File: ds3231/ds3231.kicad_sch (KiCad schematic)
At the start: 0 parts

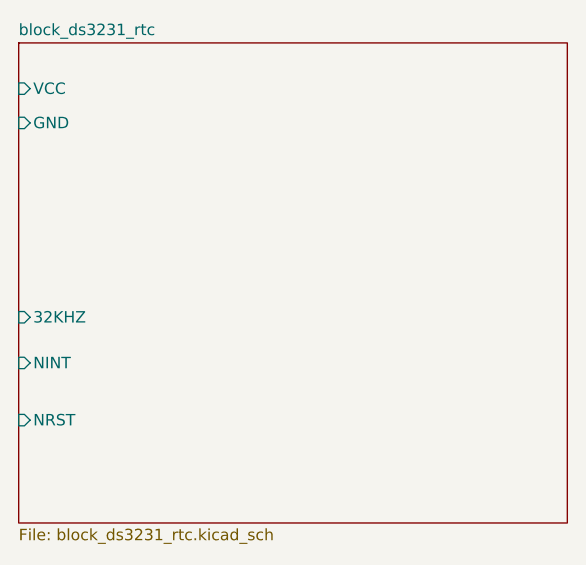
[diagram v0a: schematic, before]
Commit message: [Rushil] corrected pcb added information on both schematic and pcb user drawing correct circuit of bno055
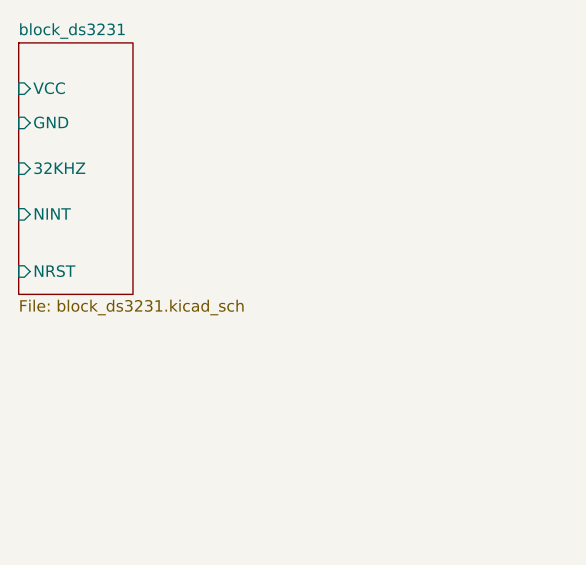
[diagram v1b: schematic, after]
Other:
- sheet block_ds3231_rtc renamed block_ds3231
- sheet block_ds3231: file block_ds3231_rtc.kicad_sch -> block_ds3231.kicad_sch
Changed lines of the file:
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@@
 	(sheet
 		(at 109.22 64.77)
-		(size 60.96 53.34)
+		(size 12.7 27.94)
 		(exclude_from_sim no)
 		(in_bom yes)
@@
 			(color 0 0 0 0.0000)
 		)
-		(property "Sheetname" "block_ds3231_rtc"
+		(property "Sheetname" "block_ds3231"
 			(at 109.22 64.0584 0)
 			(effects
@@
 			)
 		)
-		(property "Sheetfile" "block_ds3231_rtc.kicad_sch"
-			(at 109.22 118.6946 0)
+		(property "Sheetfile" "block_ds3231.kicad_sch"
+			(at 109.22 93.2946 0)
 			(effects
 				(font
@@
 		)
 		(pin "32KHZ" input
-			(at 109.22 95.25 180)
+			(at 109.22 78.74 180)
 			(effects
 				(font
@@
 		)
 		(pin "NINT" input
-			(at 109.22 100.33 180)
+			(at 109.22 83.82 180)
 			(effects
 				(font
@@
 		)
 		(pin "NRST" input
-			(at 109.22 106.68 180)
+			(at 109.22 90.17 180)
 			(effects
 				(font
@@
 		)
 		(instances
-			(project "ds3231_rtc"
+			(project "ds3231"
 				(path "/2bca7139-9750-4f0a-8cae-c77d5e9ee787"
 					(page "2")

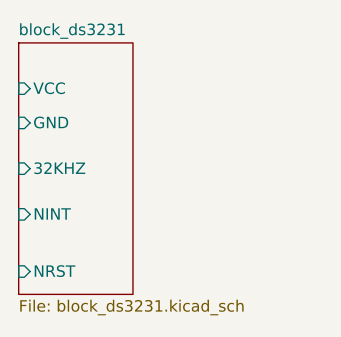
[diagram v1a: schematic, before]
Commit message: Edited and finalized blocks MCP9809 and DS3231
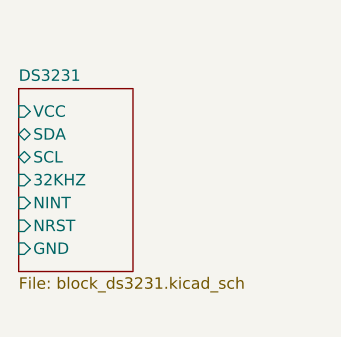
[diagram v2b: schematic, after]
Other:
- sheet block_ds3231 renamed DS3231
- sheet DS3231 ports: added SCL, SDA; removed none
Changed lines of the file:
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@@
 	(paper "A4")
 	(sheet
-		(at 109.22 64.77)
-		(size 12.7 27.94)
+		(at 109.22 69.85)
+		(size 12.7 20.32)
 		(exclude_from_sim no)
 		(in_bom yes)
@@
 			(color 0 0 0 0.0000)
 		)
-		(property "Sheetname" "block_ds3231"
-			(at 109.22 64.0584 0)
+		(property "Sheetname" "DS3231"
+			(at 109.22 69.1384 0)
 			(effects
 				(font
@@
 		)
 		(property "Sheetfile" "block_ds3231.kicad_sch"
-			(at 109.22 93.2946 0)
+			(at 109.22 90.7546 0)
 			(effects
 				(font
@@
 		)
 		(pin "32KHZ" input
-			(at 109.22 78.74 180)
+			(at 109.22 80.01 180)
 			(effects
 				(font
@@
 		)
 		(pin "GND" input
-			(at 109.22 73.66 180)
+			(at 109.22 87.63 180)
 			(effects
 				(font
@@
 		)
 		(pin "NINT" input
-			(at 109.22 83.82 180)
+			(at 109.22 82.55 180)
 			(effects
 				(font
@@
 		)
 		(pin "NRST" input
-			(at 109.22 90.17 180)
+			(at 109.22 85.09 180)
 			(effects
 				(font
@@
 		)
 		(pin "VCC" input
-			(at 109.22 69.85 180)
+			(at 109.22 72.39 180)
 			(effects
 				(font
+					(size 1.27 1.27)
+				)
+				(justify left)
+			)
+		)
+		(pin "SCL" bidirectional
+			(at 109.22 77.47 180)
+			(effects
+				(font
+					(size 1.27 1.27)
+				)
+				(justify left)
+			)
+		)
+		(pin "SDA" bidirectional
+			(at 109.22 74.93 180)
+			(effects
+				(font
